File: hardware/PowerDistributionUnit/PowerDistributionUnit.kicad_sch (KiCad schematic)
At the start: 97 parts, among them J1 973582101, J2 973582100, J3 973582101, J4 973582100, Q1 SQJ141ELP, Q2 CSD18511Q5A, SW1 SW_Push, U1 TPS25983, U2 AD5258, U3 NUCLEO_L432KC

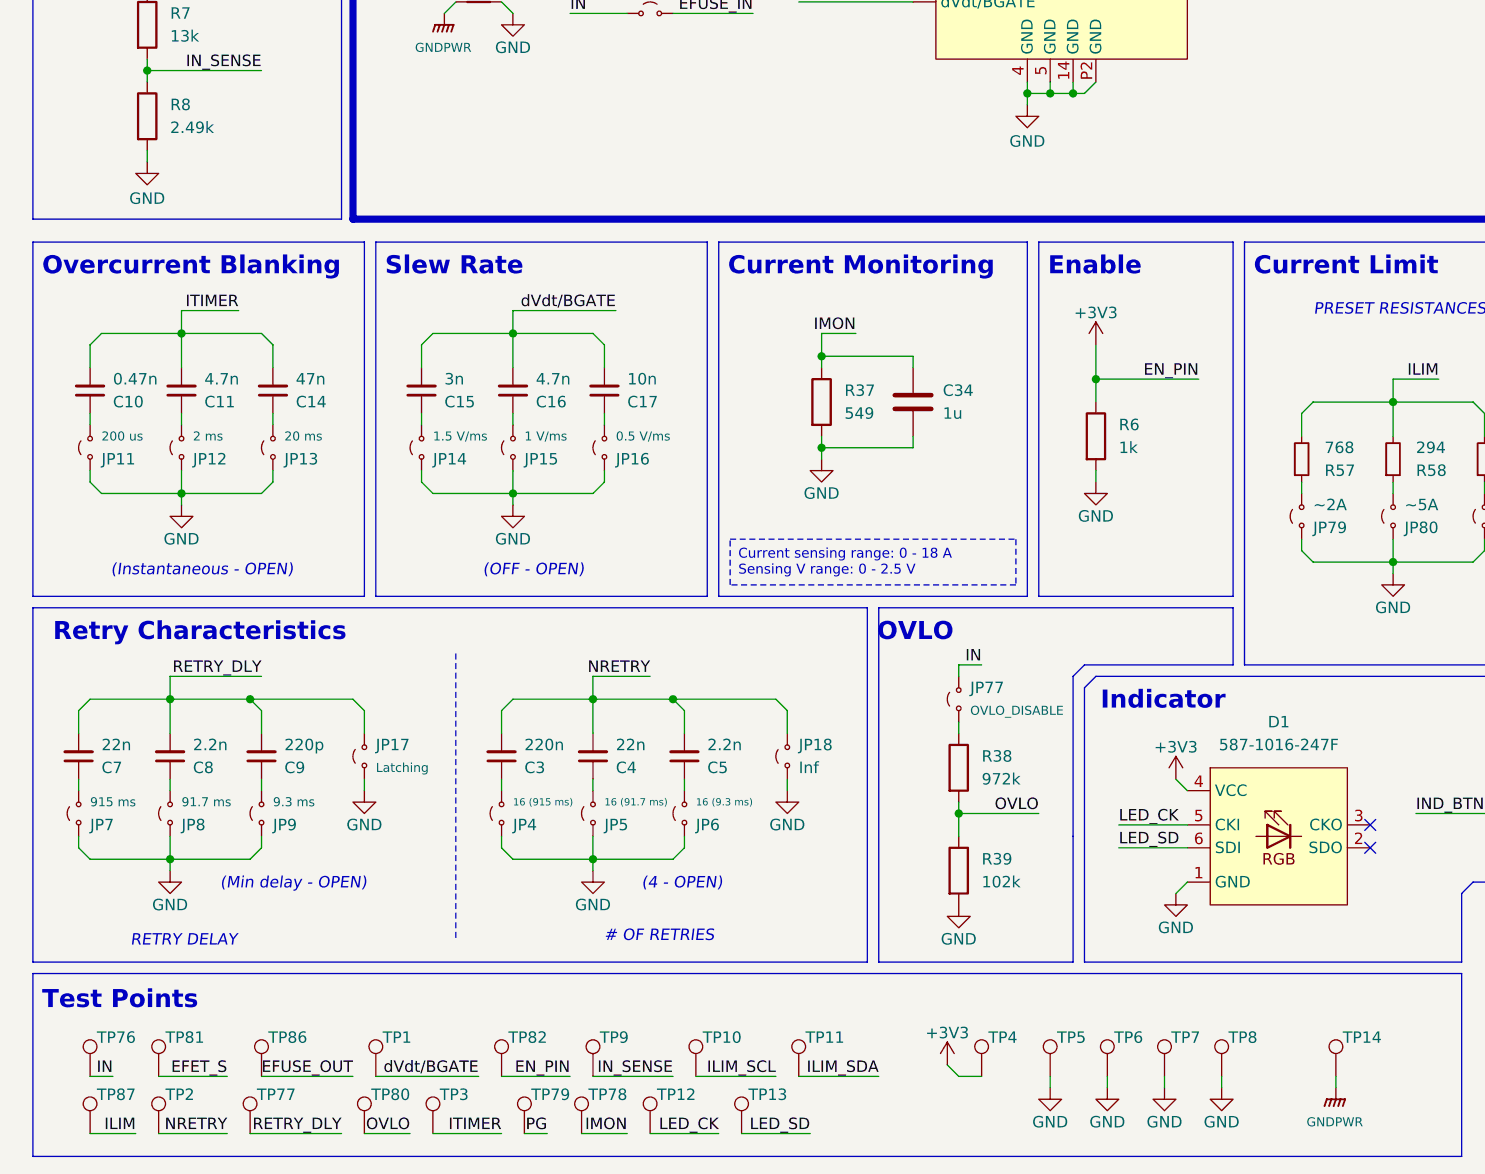
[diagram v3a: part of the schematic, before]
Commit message: modified layout, corrected en circuit, corrected uvlo labeling from disable to enable, changed more test points to gndpwr from gnd, started making some labels
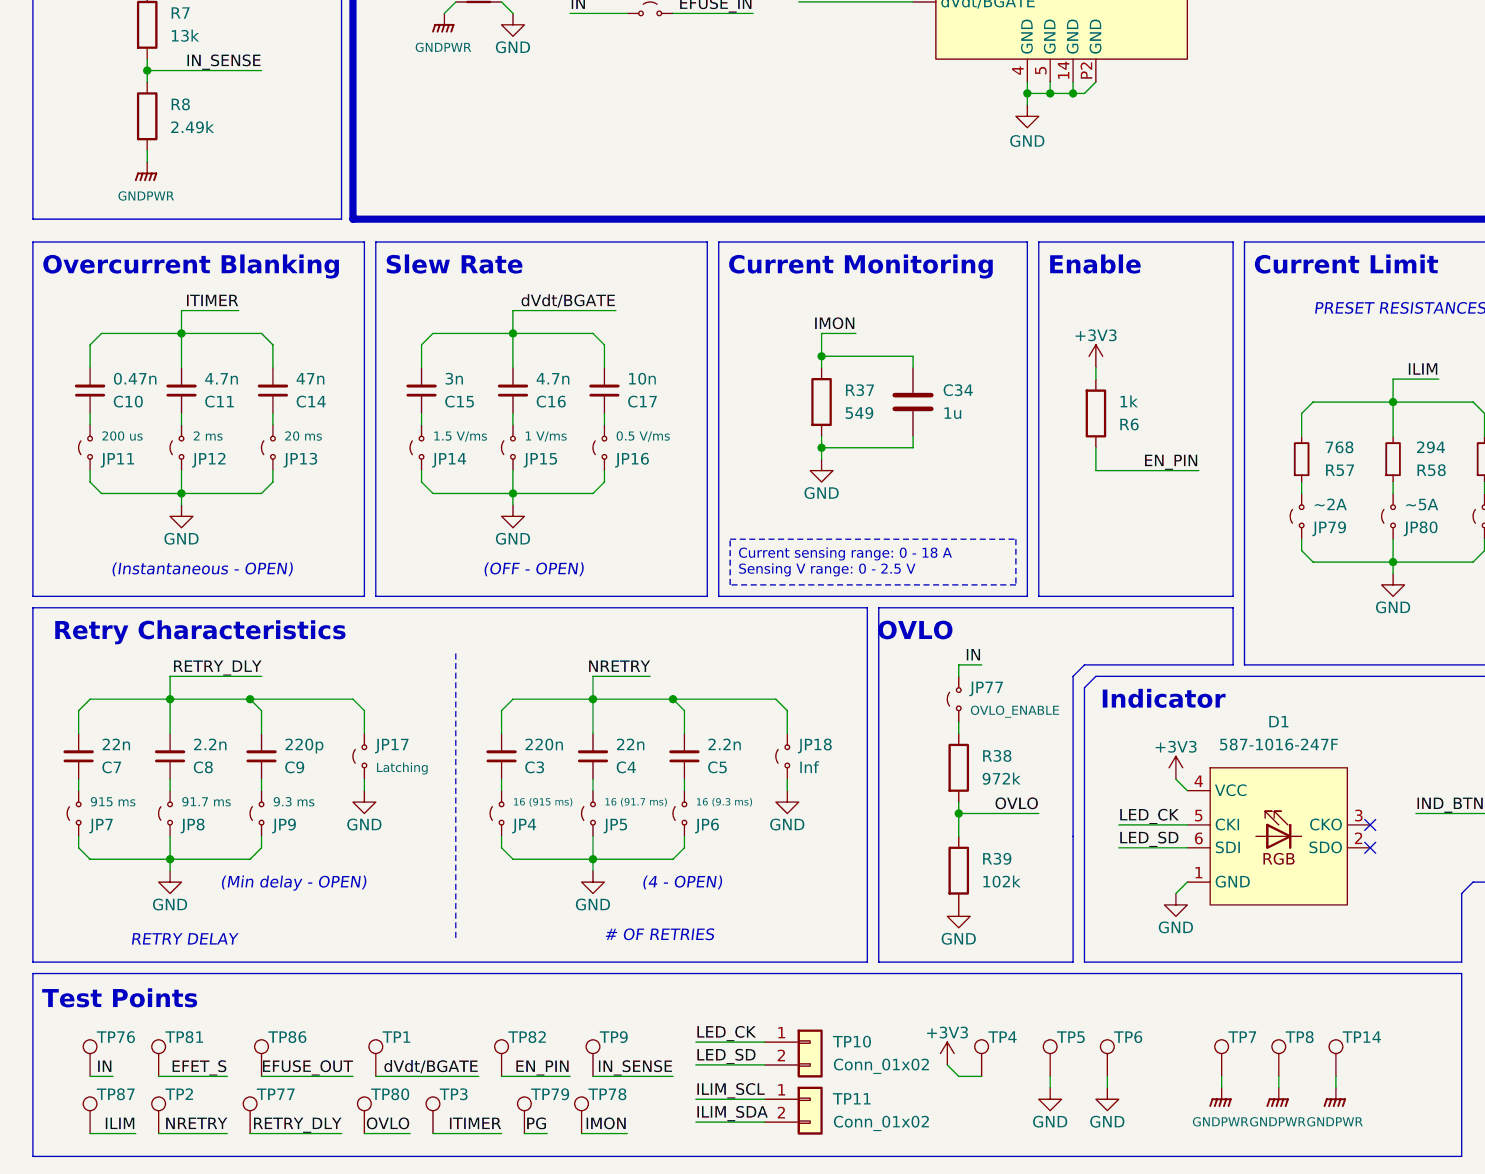
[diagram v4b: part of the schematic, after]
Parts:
- removed TP10: ILIM_SCL, Connector_PinHeader_2.54mm:PinHeader_1x01_P2.54mm_Vertical, symbol Connector:TestPoint
- removed TP11: ILIM_SDA, Connector_PinHeader_2.54mm:PinHeader_1x01_P2.54mm_Vertical, symbol Connector:TestPoint
- removed TP12: LED_CK, Connector_PinHeader_2.54mm:PinHeader_1x01_P2.54mm_Vertical, symbol Connector:TestPoint
- removed TP13: LED_SD, Connector_PinHeader_2.54mm:PinHeader_1x01_P2.54mm_Vertical, symbol Connector:TestPoint
- added TP10, TP11: Conn_01x02, Connector_PinHeader_2.54mm:PinHeader_1x02_P2.54mm_Vertical, symbol Connector_Generic:Conn_01x02
- JP77: value OVLO_DISABLE -> OVLO_ENABLE
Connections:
- net +3V3: now also R6.2; no longer JP19.2 (B), R6.1, TP82.1, U1.6 (EN/UVLO)
- net GND: no longer R6.2, R8.2, TP7.1, TP8.1
- net GNDPWR: now also R8.2, TP7.1, TP8.1
- net ILIM_SCL: now also TP11.1 (Pin_1)
- net ILIM_SDA: now also TP11.2 (Pin_2)
- net LED_CK: now also TP10.1 (Pin_1)
- net LED_SD: now also TP10.2 (Pin_2)
- new net EN_PIN: JP19.2 (B), R6.1, TP82.1, U1.6 (EN/UVLO)
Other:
- moved on the sheet: R6, TP7, TP8

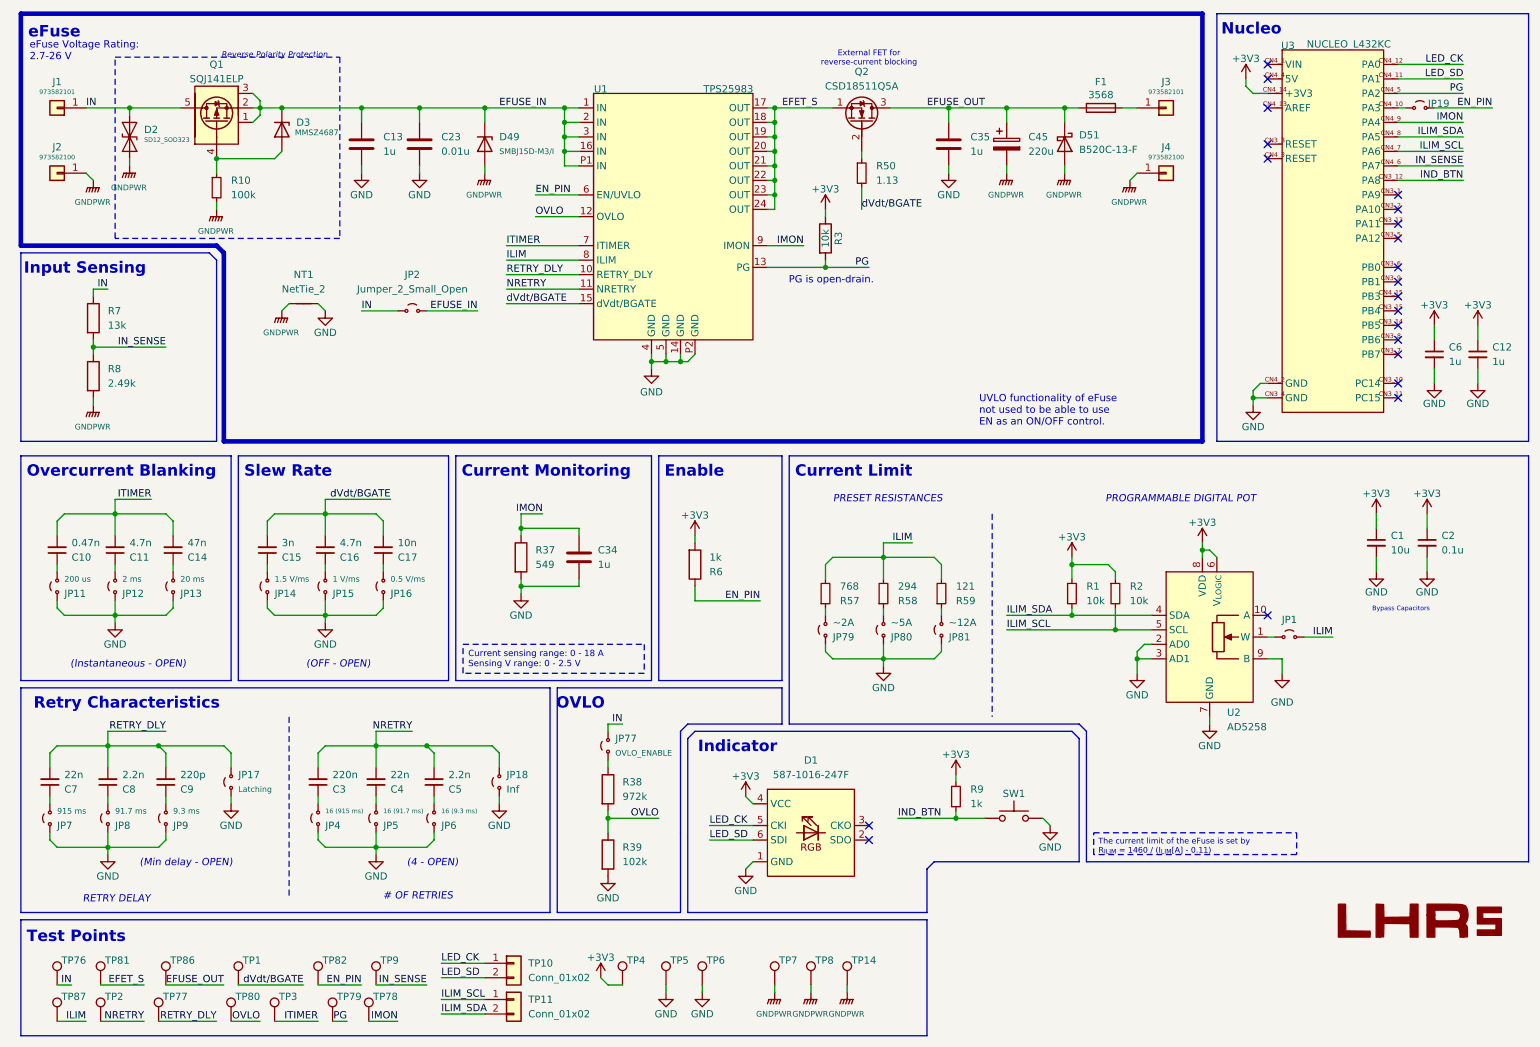
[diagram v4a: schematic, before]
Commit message: added net classes, added out test point (prev. only efuse_out)
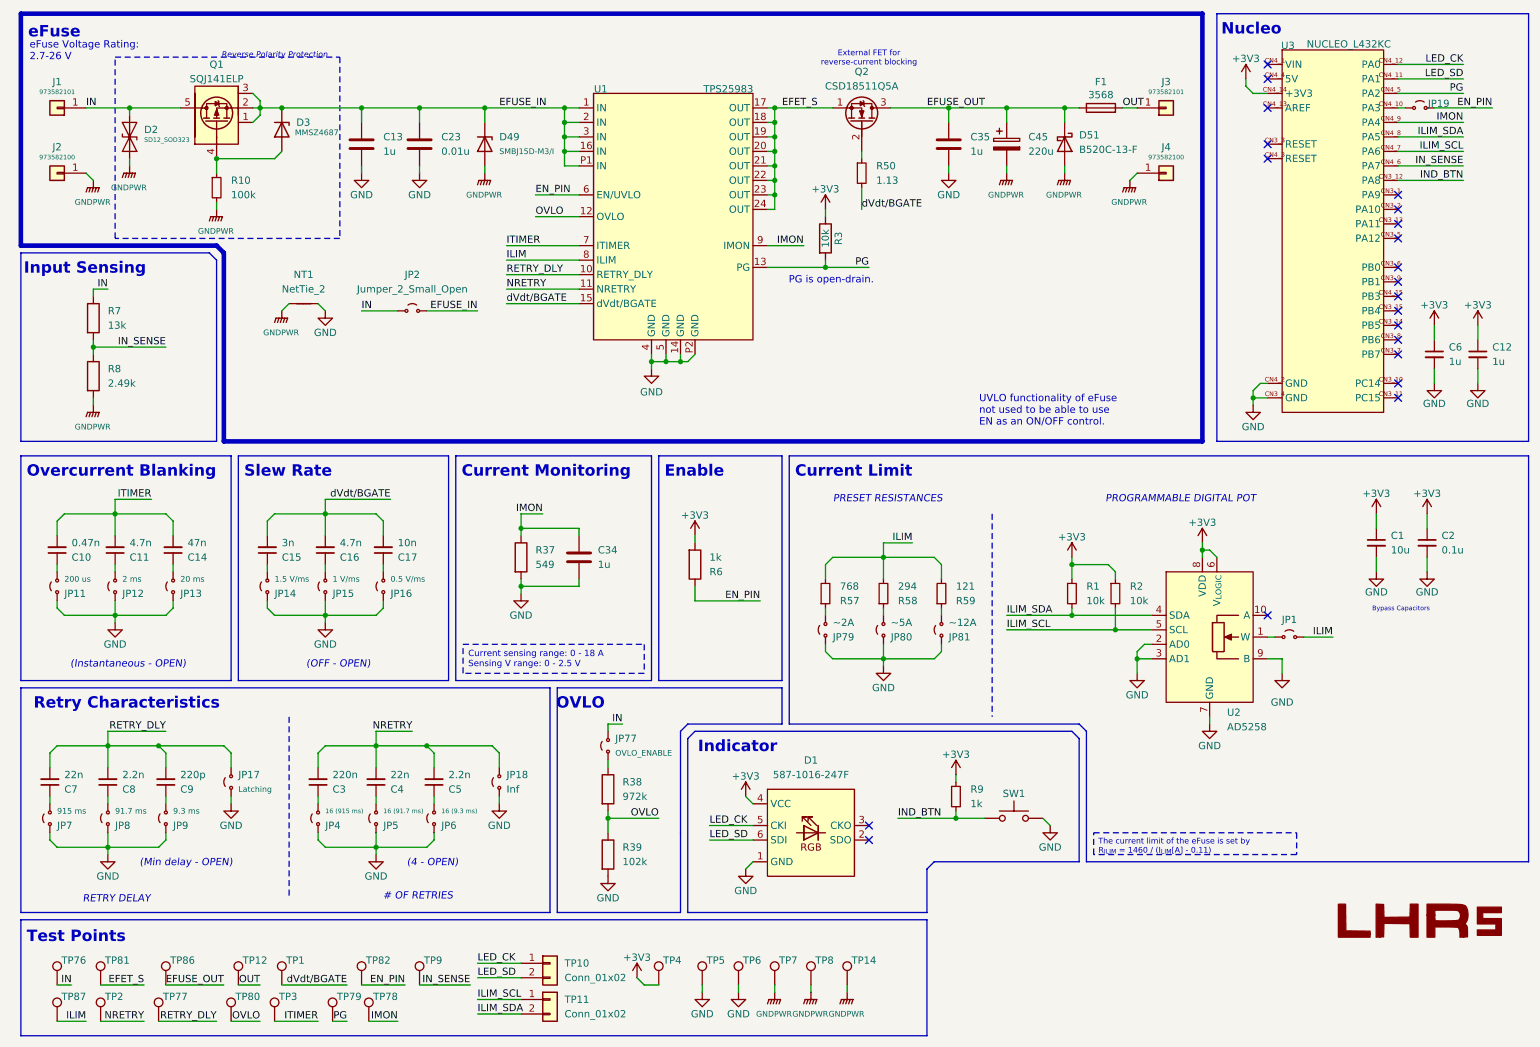
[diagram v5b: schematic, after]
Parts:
- added TP12: VOUT, TestPoint:TestPoint_Pad_D1.0mm, symbol Connector:TestPoint
- TP86: value VOUT -> EFUSE_OUT
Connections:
- net OUT: now reaches F1.2, J3.1 (Pin_1)
- net OUT: now also TP12.1
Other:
- moved on the sheet: TP1, TP10, TP11, TP4, TP5, TP6, TP82, TP9
